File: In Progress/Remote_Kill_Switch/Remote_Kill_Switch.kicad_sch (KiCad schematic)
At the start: 12 parts, among them U2 LTC4054ES5-4.2, U3 ME6211C33M5G, U4 CP2104, U5 UMH3N

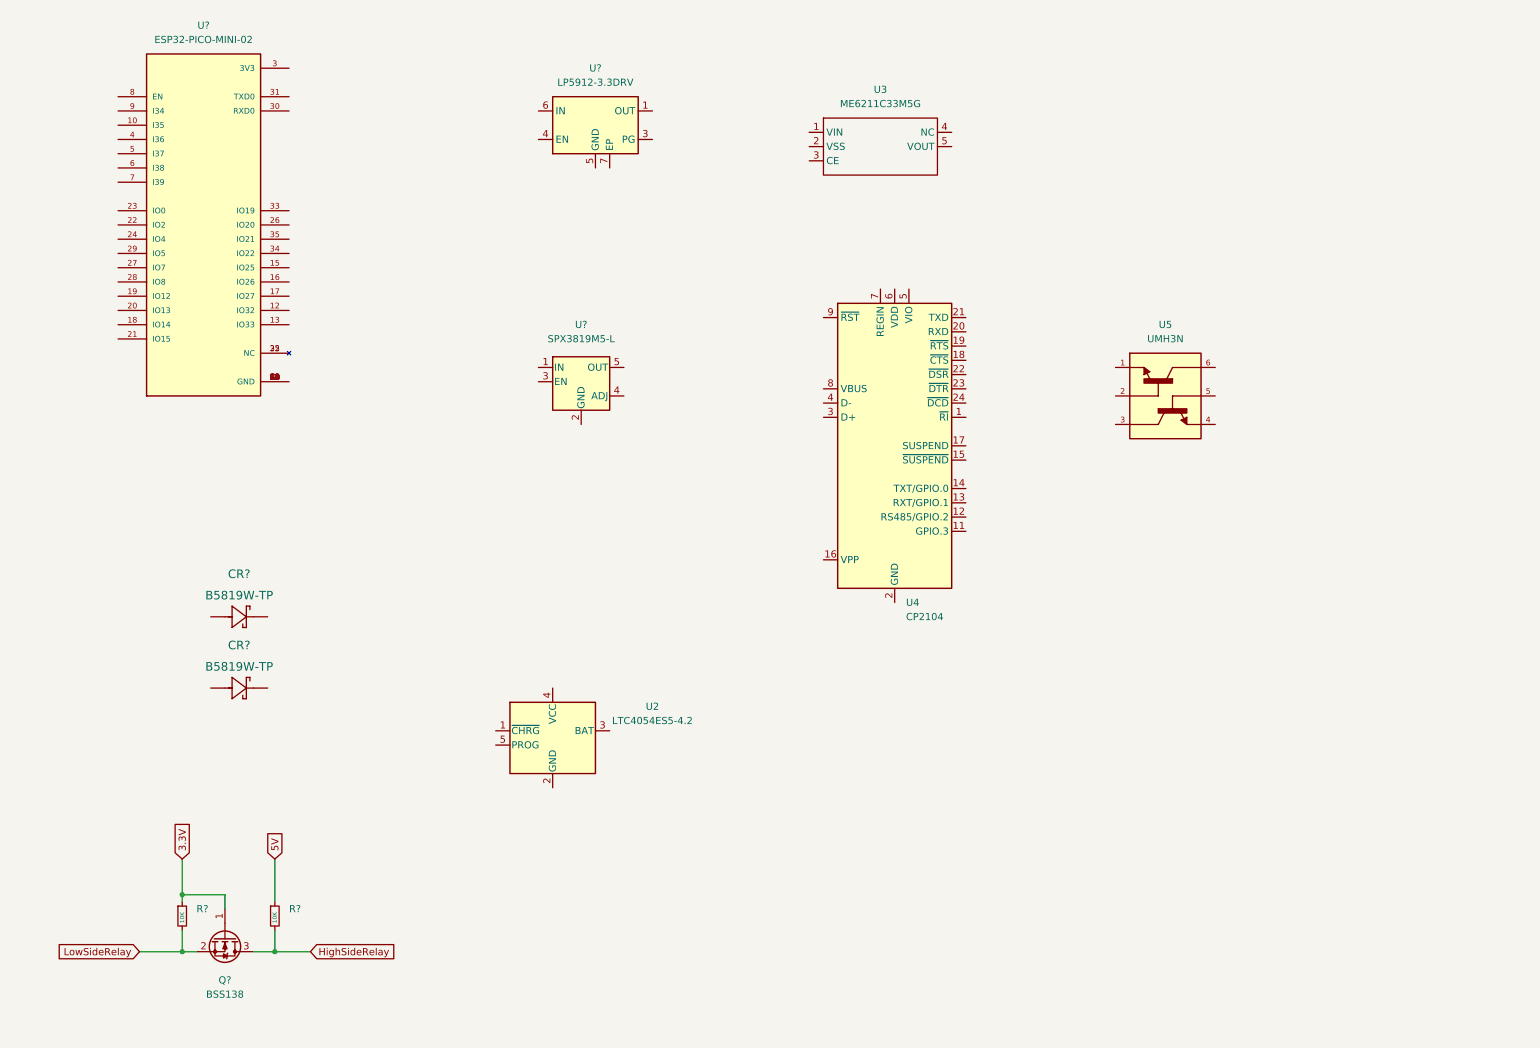
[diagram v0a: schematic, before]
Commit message: Added custom libraries and updated the Kill Switch (Remote)
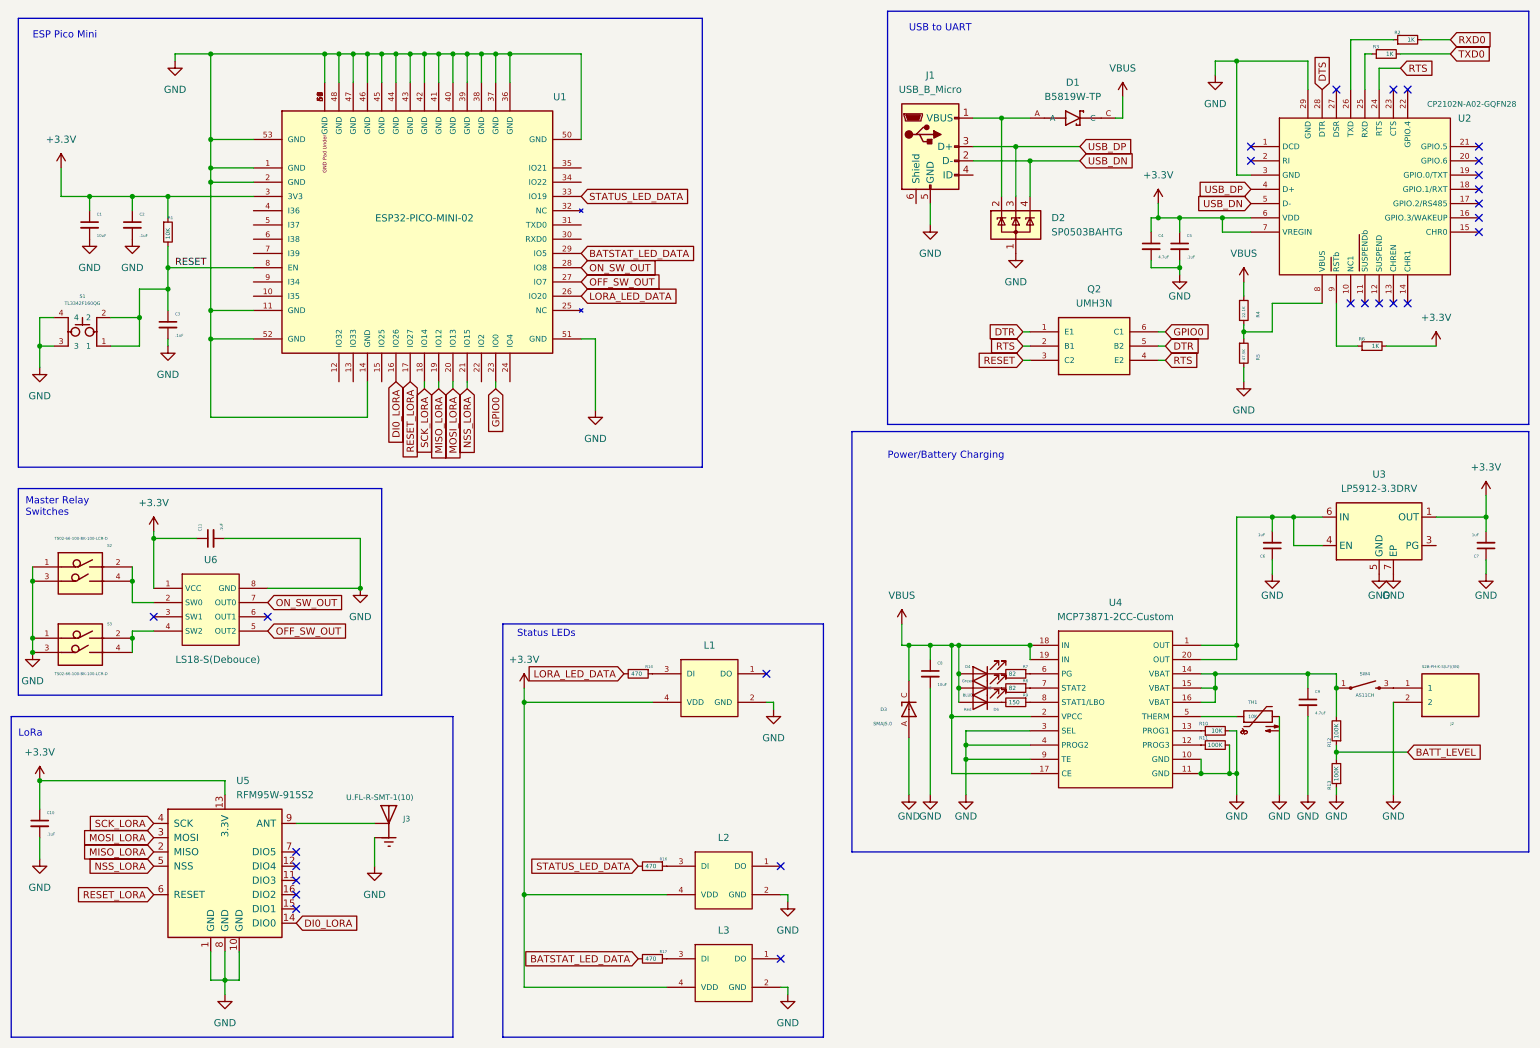
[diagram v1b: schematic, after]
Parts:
- removed CR? (x2): B5819W-TP, SDO_SOD-123_MCC, symbol Custom:B5819W-TP
- removed Q?: BSS138, Package_TO_SOT_SMD:SOT-23, symbol Transistor_FET:BSS138
- removed R? (x2): 10K, symbol Device:R_Small
- removed U2: LTC4054ES5-4.2, Package_TO_SOT_SMD:TSOT-23-5, symbol Battery_Management:LTC4054ES5-4.2
- removed U3: ME6211C33M5G, symbol Custom:ME6211C33M5G
- removed U4: CP2104, Package_DFN_QFN:QFN-24-1EP_4x4mm_P0.5mm_EP2.6x2.6mm, symbol Interface_USB:CP2104
- removed U5: UMH3N, Custom:SOT65P230X110-6N, symbol Custom:UMH3N
- removed U?: ESP32-PICO-MINI-02, Custom:MODULE_ESP32-PICO-MINI-02, symbol Custom:ESP32-PICO-MINI-02
- removed U?: SPX3819M5-L, Package_TO_SOT_SMD:SOT-23-5, symbol Regulator_Linear:SPX3819M5-L
- removed U?: LP5912-3.3DRV, Package_SON:WSON-6-1EP_2x2mm_P0.65mm_EP1x1.6mm_ThermalVias, symbol Regulator_Linear:LP5912-3.3DRV
- added C1, C8: 10uF, Capacitor_SMD:C_0805_2012Metric, symbol Device:C_Small
- added C10, C11, C2, C3, C5: .1uF, Capacitor_SMD:C_0603_1608Metric, symbol Device:C_Small
- added C4, C9: 4.7uF, Capacitor_SMD:C_0603_1608Metric, symbol Device:C_Small
- added C6, C7: 1uF, Capacitor_SMD:C_0603_1608Metric, symbol Device:C_Small
- added D1: B5819W-TP, Custom:SOD3716X135N, symbol Custom:B5819W-TP
- added D2: SP0503BAHTG, Package_TO_SOT_SMD:SOT-143, symbol Power_Protection:SP0503BAHT
- added D3: SMAJ5.0, Custom:SMAJ5.0_DIOM4325X250N, symbol Custom:SMAJ5.0
- added D4: Green, Custom:LED_0603, symbol Device:LED
- added D5: BLUE, Custom:LED_0603, symbol Device:LED
- added D6: Red, Custom:LED_0603, symbol Device:LED
- added J1: USB_B_Micro, Connector_USB:USB_Micro-B_Amphenol_10118194_Horizontal, symbol Connector:USB_B_Micro
- added J2: S2B-PH-K-S(LF)(SN), Custom:JST_S2B-PH-K-S(LF)(SN), symbol Custom:S2B-PH-K-S(LF)(SN)
- added J3: U.FL-R-SMT-1(10), Custom:HRS_U.FL-R-SMT-1(10), symbol Custom:U.FL-R-SMT-1(10)
- added L1, L2, L3: WS2812B-2020, Custom:WS2812B-2020, symbol LED:WS2812B-2020
- added Q2: UMH3N, Custom:SOT65P230X110-6N, symbol Custom:UMH3N
- added R1, R10: 10K, Resistor_SMD:R_0402_1005Metric, symbol Device:R_Small
- added R11, R12, R13: 100K, Resistor_SMD:R_0402_1005Metric, symbol Device:R_Small
- added R14, R16, R17: 470, Resistor_SMD:R_0402_1005Metric, symbol Device:R_Small
- added R2, R3, R6: 1K, Resistor_SMD:R_0402_1005Metric, symbol Device:R_Small
- added R4: 22.1K, Resistor_SMD:R_0402_1005Metric, symbol Device:R_Small
- added R5: 47.5K, Resistor_SMD:R_0402_1005Metric, symbol Device:R_Small
- added R7, R8: 82, Resistor_SMD:R_0402_1005Metric, symbol Device:R_Small
- added R9: 150, Resistor_SMD:R_0402_1005Metric, symbol Device:R_Small
- added S1: TL3342F160QG, Custom:SW_TL3342F160QG, symbol Custom:TL3342F160QG
- added S2, S3: TS02-66-100-BK-100-LCR-D, Custom:SW_TS02-66-100-BK-100-LCR-D, symbol Custom:TS02-66-100-BK-100-LCR-D
- added SW4: AS11CH, Custom:AS11CH, symbol Custom:AS11CH
- added TH1: 10K, Capacitor_SMD:C_0603_1608Metric, symbol Device:Thermistor_NTC
- added U1: ESP32-PICO-MINI-02, Custom:MODULE_ESP32-PICO-MINI-02, symbol Custom:ESP32-PICO-MINI-02
- added U2: CP2102N-A02-GQFN28, Package_DFN_QFN:QFN-28-1EP_5x5mm_P0.5mm_EP3.35x3.35mm, symbol Custom:CP2102N-A02-GQFN28
- added U3: LP5912-3.3DRV, Package_SON:WSON-6-1EP_2x2mm_P0.65mm_EP1x1.6mm_ThermalVias, symbol Regulator_Linear:LP5912-3.3DRV
- added U4: MCP73871-2CC-Custom, Package_DFN_QFN:QFN-20-1EP_4x4mm_P0.5mm_EP2.7x2.7mm_ThermalVias, symbol Custom:MCP73871-2CC-Custom
- added U5: RFM95W-915S2, Custom:RFM95W-915S2, symbol RF_Module:RFM95W-915S2
- added U6: LS18-S(Debouce), Custom:SOIC127P600X175-8N, symbol Custom:LS18-S(Debouce)
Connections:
- new net: L1.3 (DI), R14.1
- new net: J2.1, SW4.3
- new net: R9.1, U4.8 (STAT1/LBO)
- new net: D6.1 (K), R9.2
- new net: L3.3 (DI), R17.1
- new net: C6.2, U3.4 (EN), U3.6 (IN), U4.1 (OUT), U4.20 (OUT)
- new net: L2.3 (DI), R16.1
- new net: D4.1 (K), R7.2
- new net: R7.1, U4.6 (PG)
- new net: R11.1, U4.12 (PROG3)
- new net: R10.1, U4.13 (PROG1)
- new net: C9.1, R12.2, SW4.1, U4.14 (VBAT), U4.15 (VBAT), U4.16 (VBAT)
- new net: TH1.1, U4.5 (THERM)
- new net: R8.1, U4.7 (STAT2)
- new net: R3.1, U2.25 (RXD)
- new net: R2.1, U2.26 (TXD)
- new net: R4.2, R5.1, U2.8 (VBUS)
- new net: R6.1, U2.9 (RSTb)
- new net: D1.A, D2.2 (K), J1.1 (VBUS)
- new net: J3.2, U5.9 (ANT)
- new net: D5.1 (K), R8.2
- new net: S3.2, S3.4, U6.4 (SW2)
- new net: S2.2, S2.4, U6.2 (SW0)
- new net +3V3: C1.1, C10.1, C11.1, C2.1, C4.1, C5.1, C7.2, L1.4 (VDD), L2.4 (VDD), L3.4 (VDD), R1.1, R6.2, U1.3 (3V3), U2.6 (VDD), U2.7 (VREGIN), U3.1 (OUT), U5.13 (3.3V), U6.1 (VCC)
- new net BATSTAT_LED_DATA: R17.2, U1.29 (IO5)
- new net BATT_LEVEL: R12.1, R13.2
- new net DI0_LORA: U1.16 (IO26), U5.14 (DIO0)
- new net DTR: Q2.1 (E1), Q2.5 (B2)
- new net DTS: U2.28 (DTR)
- new net GND: C1.2, C10.2, C11.2, C2.2, C3.2, C4.2, C5.2, C6.1, C7.1, C8.2, C9.2, D2.1 (A), D3.A, J1.5 (GND), J2.2, J3.1, J3.3, L1.2 (GND), L2.2 (GND), L3.2 (GND), R10.2, R11.2, R13.1, R5.2, S1.3, S1.4, S2.1, S2.3, S3.1, S3.3, TH1.2, U1.1 (GND), U1.11 (GND), U1.14 (GND), U1.2 (GND), U1.36 (GND), U1.37 (GND), U1.38 (GND), U1.39 (GND), U1.40 (GND), U1.41 (GND), U1.42 (GND), U1.43 (GND), U1.44 (GND), U1.45 (GND), U1.46 (GND), U1.47 (GND), U1.48 (GND), U1.49 (GND), U1.50 (GND), U1.51 (GND), U1.52 (GND), U1.53 (GND), U1.54 (GND), U1.55 (GND), U1.56 (GND), U1.57 (GND), U1.58 (GND), U1.59 (GND), U1.60 (GND), U1.61 (GND), U2.29 (GND), U2.3 (GND), U3.5 (GND), U3.7 (EP), U4.10 (GND), U4.11 (GND), U4.3 (SEL), U4.4 (PROG2), U4.9 (TE), U5.1 (GND), U5.10 (GND), U5.8 (GND), U6.8 (GND)
- new net GPIO0: Q2.6 (C1), U1.23 (IO0)
- new net LORA_LED_DATA: R14.2, U1.26 (IO20)
- new net MISO_LORA: U1.19 (IO12), U5.2 (MISO)
- new net MOSI_LORA: U1.20 (IO13), U5.3 (MOSI)
- new net NSS_LORA: U1.21 (IO15), U5.5 (NSS)
- new net OFF_SW_OUT: U1.27 (IO7), U6.5 (OUT2)
- new net ON_SW_OUT: U1.28 (IO8), U6.7 (OUT0)
- new net RESET: C3.1, Q2.3 (C2), R1.2, S1.1, S1.2, U1.8 (EN)
- new net RESET_LORA: U1.17 (IO27), U5.6 (RESET)
- new net RTS: Q2.2 (B1), Q2.4 (E2), U2.24 (RTS)
- new net RXD0: R2.2
- new net SCK_LORA: U1.18 (IO14), U5.4 (SCK)
- new net STATUS_LED_DATA: R16.2, U1.33 (IO19)
- new net TXD0: R3.2
- new net USB_DN: D2.4 (K), J1.2 (D-), U2.5 (D-)
- new net USB_DP: D2.3 (K), J1.3 (D+), U2.4 (D+)
- new net VBUS: C8.1, D1.C, D3.C, D4.2 (A), D5.2 (A), D6.2 (A), R4.1, U4.17 (CE), U4.18 (IN), U4.19 (IN), U4.2 (VPCC)
- no-connect marks 0 -> 27
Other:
- note added: "ESP Pico Mini"
- note added: "LoRa"
- note added: "Master Relay Switches"
- note added: "Power/Battery Charging"
- note added: "Status LEDs"
- note added: "USB to UART"
